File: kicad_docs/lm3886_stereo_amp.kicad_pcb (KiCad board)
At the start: 2 copper layers, 53.3 x 30.5 mm, 22 parts, among them J1 signal_in, J2 speaker_out, J3 power_in, U1 LM3886

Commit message: create directory structure, add pics and readme
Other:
- board text added: "github.com/JordanAceto/LM3886_power_amp_pcb rev 1 2020-02-23"
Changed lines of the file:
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@@
-(kicad_pcb (version 20171130) (host pcbnew 5.1.2-f72e74a~84~ubuntu18.04.1)
+(kicad_pcb (version 20171130) (host pcbnew 5.1.5-52549c5~84~ubuntu18.04.1)
   (general
     (thickness 1.6)
-    (drawings 12)
+    (drawings 13)
     (tracks 69)
     (zones 0)
@@
   )
   (setup
-    (last_trace_width 1.143)
+    (last_trace_width 0.25)
     (user_trace_width 0.762)
     (user_trace_width 1.143)
@@
     )
   )
+  (gr_text "github.com/JordanAceto/LM3886_power_amp_pcb\nrev 1\n2020-02-23" (at 100.33 39.37) (layer B.SilkS)
+    (effects (font (size 1 1) (thickness 0.15)) (justify left mirror))
+  )
   (gr_line (start 48.26 53.34) (end 101.6 53.34) (layer Edge.Cuts) (width 0.05))
   (gr_text LM3886 (at 77.978 33.274) (layer F.SilkS)
@@
   (segment (start 80.881 34.925) (end 80.206 34.925) (width 0.25) (layer F.Cu) (net 7))
   (segment (start 80.206 34.925) (end 78.359 34.925) (width 0.25) (layer F.Cu) (net 7))
-  (segment (start 73.152 43.307) (end 75.946 43.307) (width 1.143) (layer F.Cu) (net 8))
-  (segment (start 69.723 49.53) (end 69.723 46.736) (width 1.143) (layer F.Cu) (net 8))
-  (segment (start 69.723 46.736) (end 73.152 43.307) (width 1.143) (layer F.Cu) (net 8))
+  (segment (start 69.723 49.53) (end 69.723 46.736) (width 1.143) (layer F.Cu) (net 8) (status 1000000))
+  (segment (start 73.152 43.307) (end 75.946 43.307) (width 1.143) (layer F.Cu) (net 8) (status 1000000))
+  (segment (start 69.723 46.736) (end 73.152 43.307) (width 1.143) (layer F.Cu) (net 8) (status 1000000))
   (segment (start 75.369001 30.596001) (end 76.269 31.496) (width 1.143) (layer F.Cu) (net 9))
   (segment (start 74.597499 29.824499) (end 75.369001 30.596001) (width 1.143) (layer F.Cu) (net 9))
@@
   (segment (start 76.298 34.925) (end 72.869 31.496) (width 1.143) (layer F.Cu) (net 11))
   (segment (start 76.309 34.925) (end 76.298 34.925) (width 1.143) (layer F.Cu) (net 11))
-  (segment (start 77.70501 39.647646) (end 76.309 38.251636) (width 1.143) (layer F.Cu) (net 11))
-  (segment (start 75.184 48.701136) (end 77.70501 46.180126) (width 1.143) (layer F.Cu) (net 11))
-  (segment (start 77.70501 46.180126) (end 77.70501 39.647646) (width 1.143) (layer F.Cu) (net 11))
-  (segment (start 75.184 48.768) (end 75.184 48.701136) (width 1.143) (layer F.Cu) (net 11))
+  (segment (start 77.70501 39.647646) (end 76.309 38.251636) (width 1.143) (layer F.Cu) (net 11) (status 1000000))
+  (segment (start 75.184 48.768) (end 75.184 48.701136) (width 1.143) (layer F.Cu) (net 11) (status 1000000))
+  (segment (start 75.184 48.701136) (end 77.70501 46.180126) (width 1.143) (layer F.Cu) (net 11) (status 1000000))
+  (segment (start 77.70501 46.180126) (end 77.70501 39.647646) (width 1.143) (layer F.Cu) (net 11) (status 1000000))
   (segment (start 89.408 26.162) (end 87.884 24.638) (width 0.25) (layer F.Cu) (net 12))
   (segment (start 81.534 26.251) (end 81.369 26.416) (width 0.25) (layer F.Cu) (net 12))
@@
     )
   )
+  (zone (net 0) (net_name "") (layer B.Cu) (hatch edge 0.508)
+    (connect_pads (clearance 0.508))
+    (min_thickness 0.254)
+    (keepout (tracks not_allowed) (vias not_allowed) (copperpour not_allowed))
+    (fill (arc_segments 32) (thermal_gap 0.508) (thermal_bridge_width 0.508))
+    (polygon
+      (pts
+        (xy 80.01 30.226) (xy 80.01 22.733) (xy 80.391 22.733) (xy 80.391 30.48)
+      )
+    )
+  )
+  (zone (net 0) (net_name "") (layer B.Cu) (hatch edge 0.508)
+    (connect_pads (clearance 0.508))
+    (min_thickness 0.254)
+    (keepout (tracks not_allowed) (vias not_allowed) (copperpour not_allowed))
+    (fill (arc_segments 32) (thermal_gap 0.508) (thermal_bridge_width 0.508))
+    (polygon
+      (pts
+        (xy 82.677 53.467) (xy 82.677 32.766) (xy 83.185 32.766) (xy 83.312 32.766) (xy 83.312 53.467)
+      )
+    )
+  )
   (zone (net 0) (net_name "") (layer F.Cu) (hatch edge 0.508)
     (connect_pads (clearance 0.508))
@@
       )
     )
-  )
-  (zone (net 0) (net_name "") (layer F.Cu) (hatch edge 0.508)
-    (connect_pads (clearance 0.508))
-    (min_thickness 0.254)
-    (keepout (tracks not_allowed) (vias not_allowed) (copperpour not_allowed))
-    (fill (arc_segments 32) (thermal_gap 0.508) (thermal_bridge_width 0.508))
-    (polygon
-      (pts
-        (xy 77.47 47.752) (xy 77.47 53.467) (xy 76.962 53.467) (xy 76.962 47.752)
-      )
-    )
-  )
-  (zone (net 0) (net_name "") (layer B.Cu) (hatch edge 0.508)
-    (connect_pads (clearance 0.508))
-    (min_thickness 0.254)
-    (keepout (tracks not_allowed) (vias not_allowed) (copperpour not_allowed))
-    (fill (arc_segments 32) (thermal_gap 0.508) (thermal_bridge_width 0.508))
-    (polygon
-      (pts
-        (xy 80.01 30.226) (xy 80.01 22.733) (xy 80.391 22.733) (xy 80.391 30.48)
-      )
-    )
-  )
-  (zone (net 0) (net_name "") (layer B.Cu) (hatch edge 0.508)
-    (connect_pads (clearance 0.508))
-    (min_thickness 0.254)
-    (keepout (tracks not_allowed) (vias not_allowed) (copperpour not_allowed))
-    (fill (arc_segments 32) (thermal_gap 0.508) (thermal_bridge_width 0.508))
-    (polygon
-      (pts
-        (xy 76.962 53.467) (xy 76.962 32.639) (xy 77.597 31.877) (xy 77.597 53.467)
-      )
-    )
-  )
-  (zone (net 0) (net_name "") (layer B.Cu) (hatch edge 0.508)
-    (connect_pads (clearance 0.508))
-    (min_thickness 0.254)
-    (keepout (tracks not_allowed) (vias not_allowed) (copperpour not_allowed))
-    (fill (arc_segments 32) (thermal_gap 0.508) (thermal_bridge_width 0.508))
-    (polygon
-      (pts
-        (xy 82.677 53.467) (xy 82.677 32.766) (xy 83.185 32.766) (xy 83.312 32.766) (xy 83.312 53.467)
-      )
-    )

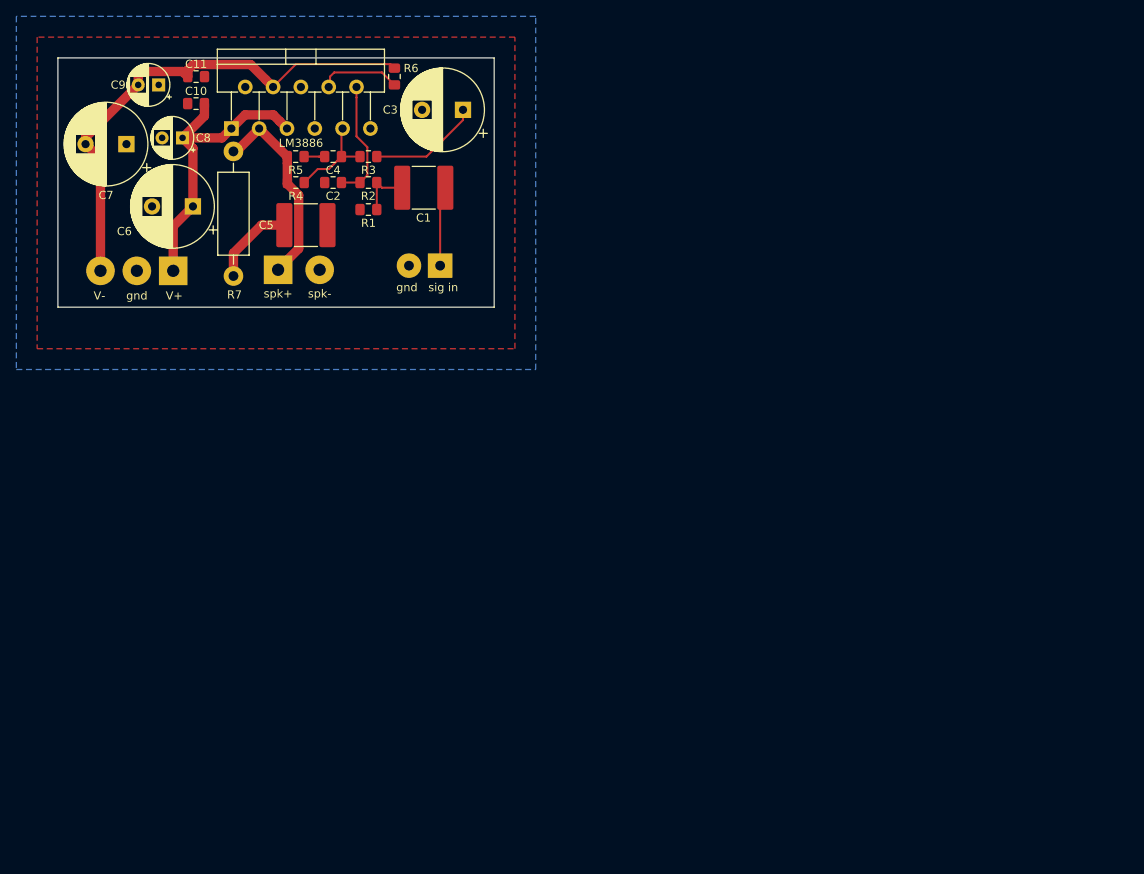
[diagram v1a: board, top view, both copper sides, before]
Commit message: redesign pcb for easier to source components
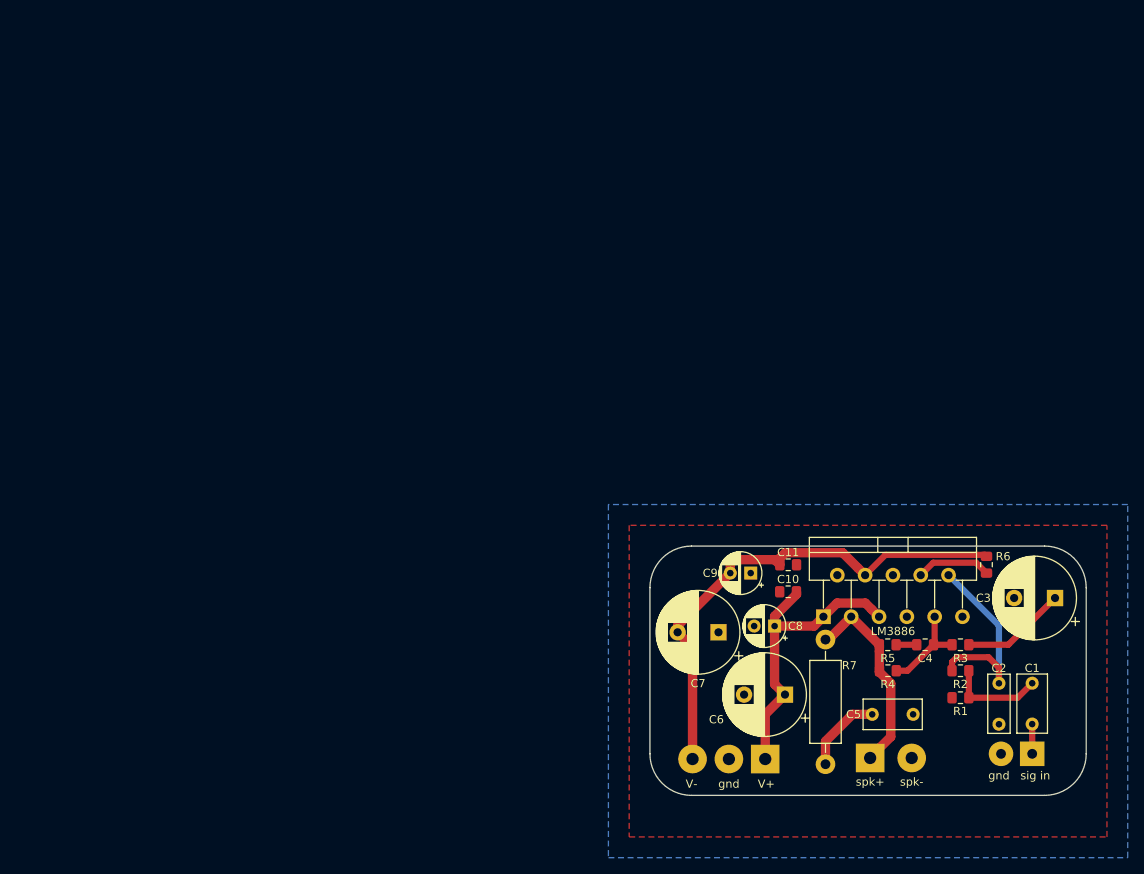
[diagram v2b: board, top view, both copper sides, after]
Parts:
- C1, C5: footprint Capacitor_SMD:C_2220_5650Metric_Pad1.97x5.40mm_HandSolder -> Capacitor_THT:C_Rect_L7.0mm_W3.5mm_P5.00mm
- C2: footprint Capacitor_SMD:C_0805_2012Metric_Pad1.15x1.40mm_HandSolder -> Capacitor_THT:C_Rect_L7.0mm_W2.5mm_P5.00mm
- C3: value 100uF -> 47uF
- moved C2 101.9 mm to (163.3, 99.3), turned to 270 degrees
- moved C1 95.9 mm to (167.4, 99.3), turned to 270 degrees
- moved U1 93.8 mm to (141.9, 91.2)
- moved C11 93.8 mm to (137.6, 84.8)
- moved C7 93.8 mm to (129.0, 93.1)
- moved J2 93.8 mm to (147.6, 108.5)
- moved J3 93.8 mm to (134.7, 108.6)
- moved C10 93.8 mm to (137.5, 88.1)
- moved C3 93.8 mm to (170.2, 88.9)
- moved C6 93.8 mm to (137.2, 100.7)
- moved J1 93.8 mm to (167.4, 108.0)
- moved R1 93.8 mm to (158.6, 101.1)
- moved R2 93.8 mm to (158.6, 97.8)
- moved R3 93.8 mm to (158.6, 94.6)
- moved R6 93.8 mm to (161.8, 84.8)
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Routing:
- net Net-(C2-Pad1): track 14.9 -> 25.4 mm
- net Net-(C1-Pad2): track 9.79 -> 3.64 mm
- net Net-(C1-Pad1): track 6.67 -> 11.8 mm
- net Net-(R6-Pad2): track 10.1 -> 9.20 mm
- net Net-(C3-Pad1): track 13.6 -> 12.9 mm
- net Net-(C5-Pad1): track 10.4 -> 9.88 mm
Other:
- outline, holes or cut-outs redrawn
- board text removed: "github.com/JordanAceto/LM3886_power_amp_pcb rev 1 2020-02-23"
